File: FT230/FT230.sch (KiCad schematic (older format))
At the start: 19 parts, among them J1 USB_B_Micro, J2 Conn_01x04, J3 Conn_01x02, J4 Conn_01x02, U1 FT230XQ

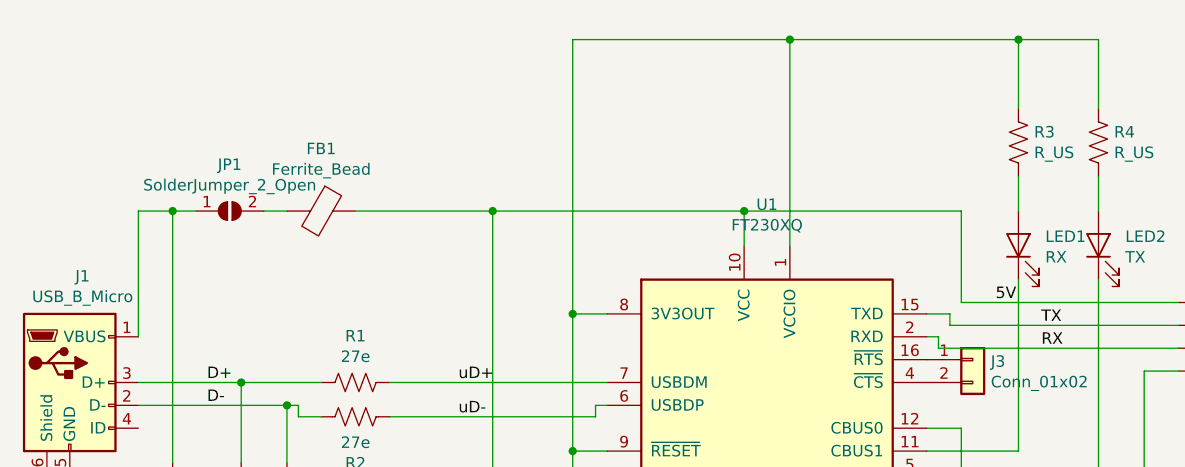
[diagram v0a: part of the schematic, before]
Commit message: Silkscreens Updated
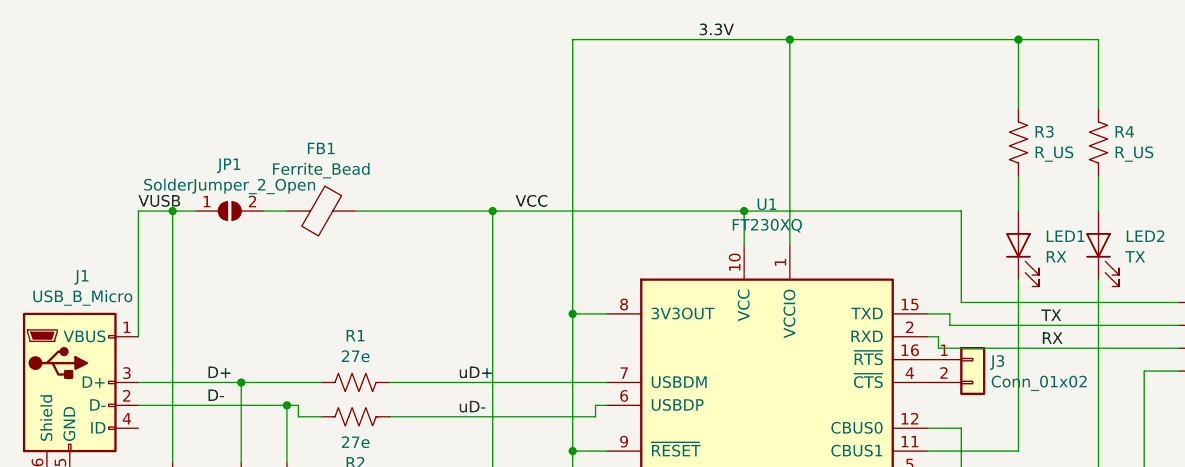
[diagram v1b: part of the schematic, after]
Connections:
- net 3.3V: now reaches C6.1, R3.1, R4.1, U1.1 (VCCIO), U1.8 (3V3OUT), U1.9 (~RESET)
- net VUSB: now reaches C1.1, J1.1 (VBUS), JP1.1 (A)
- net 5V renamed VCC
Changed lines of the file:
@@
 Text Label 6000 2950 0    50   ~ 0
 TX
-Text Label 5800 2850 0    50   ~ 0
-5V
+Text Label 2050 2450 0    50   ~ 0
+VUSB
 Wire Wire Line
 	6450 3150 6450 4200
@@
 Wire Wire Line
 	4700 2450 5650 2450
+Text Label 4500 1700 0    50   ~ 0
+3.3V
+Text Label 3700 2450 0    50   ~ 0
+VCC
 $EndSCHEMATC

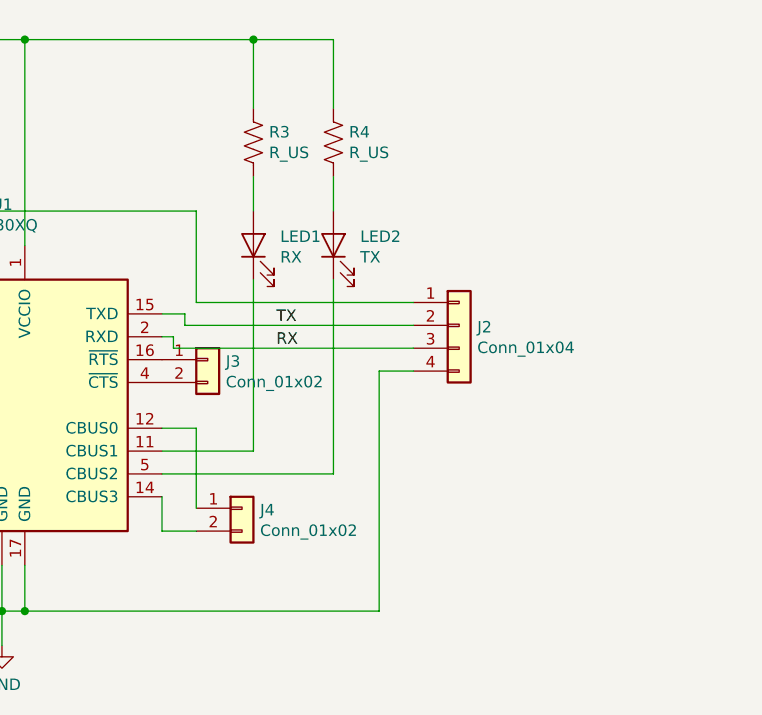
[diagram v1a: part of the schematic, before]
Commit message: Power LED Added
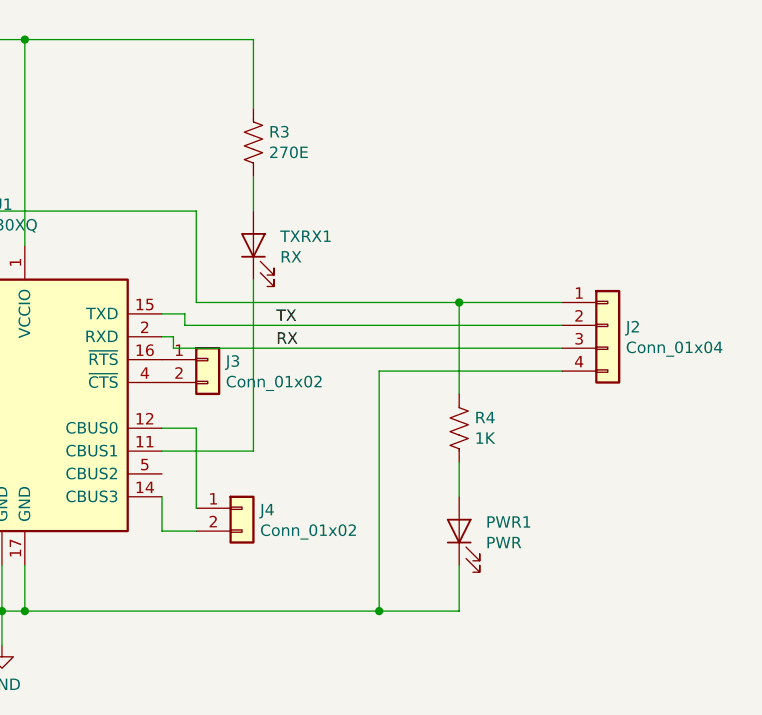
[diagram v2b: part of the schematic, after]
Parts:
- PWR1: renamed from LED2; value TX -> PWR
- R3: value R_US -> 270E
- R4: value R_US -> 1K
- renumbered LED1 to TXRX1
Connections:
- net 3.3V: no longer R4.1
- net GND: now also PWR1.1 (K)
- net VCC: now also R4.1
- net at U1.5 (CBUS2): no longer PWR1.1 (K)
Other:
- moved on the sheet: J2, PWR1, R4
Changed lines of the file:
@@
-$EndComp
-$Comp
-L Device:R_US R4
-U 1 1 5D279F68
-P 6250 2150
-F 0 "R4" H 6318 2195 50  0000 L CNN
-F 1 "R_US" H 6318 2105 50  0000 L CNN
-F 2 "Resistor_SMD:R_0805_2012Metric_Pad1.15x1.40mm_HandSolder" V 6290 2140 50  0001 C CNN
-F 3 "~" H 6250 2150 50  0001 C CNN
-	1    6250 2150
-	1    0    0    -1
 $EndComp
 $Comp
@@
 	4700 4200 4700 4000
 $Comp
-L Device:LED LED2
-U 1 1 5D27B0C2
-P 6250 2600
-F 0 "LED2" V 6288 2483 50  0000 R CNN
-F 1 "TX" V 6198 2483 50  0000 R CNN
-F 2 "LED_SMD:LED_0805_2012Metric_Castellated" H 6250 2600 50  0001 C CNN
-F 3 "~" H 6250 2600 50  0001 C CNN
-	1    6250 2600
-	0    -1   -1   0
-$EndComp
-$Comp
 L Device:R_US R3
 U 1 1 5D282FE6
 P 5900 2150
 F 0 "R3" H 5968 2195 50  0000 L CNN
-F 1 "R_US" H 5968 2105 50  0000 L CNN
+F 1 "270E" H 5968 2105 50  0000 L CNN
 F 2 "Resistor_SMD:R_0805_2012Metric_Pad1.15x1.40mm_HandSolder" V 5940 2140 50  0001 C CNN
 F 3 "~" H 5900 2150 50  0001 C CNN
@@
 $EndComp
 $Comp
-L Device:LED LED1
+L Device:LED TXRX1
 U 1 1 5D282FEC
 P 5900 2600
-F 0 "LED1" V 5938 2483 50  0000 R CNN
+F 0 "TXRX1" V 5938 2483 50  0000 R CNN
 F 1 "RX" V 5848 2483 50  0000 R CNN
 F 2 "LED_SMD:LED_0805_2012Metric_Castellated" H 5900 2600 50  0001 C CNN
@@
 	5900 3500 5500 3500
 Wire Wire Line
-	6250 2300 6250 2450
-Wire Wire Line
-	6250 2750 6250 3600
-Wire Wire Line
-	6250 3600 5500 3600
-Wire Wire Line
 	4900 2600 4900 1700
 Wire Wire Line
 	4900 1700 5900 1700
 Wire Wire Line
-	6250 1700 6250 2000
-Wire Wire Line
 	5900 2000 5900 1700
-Connection ~ 5900 1700
-Wire Wire Line
-	5900 1700 6250 1700
 Wire Wire Line
 	4100 3500 3950 3500
@@
 L Connector_Generic:Conn_01x04 J2
 U 1 1 5D2DAFBA
-P 6800 2950
-F 0 "J2" H 6879 2942 50  0000 L CNN
-F 1 "Conn_01x04" H 6879 2852 50  0000 L CNN
-F 2 "Connector_PinHeader_2.54mm:PinHeader_1x04_P2.54mm_Horizontal" H 6800 2950 50  0001 C CNN
-F 3 "~" H 6800 2950 50  0001 C CNN
-	1    6800 2950
+P 7450 2950
+F 0 "J2" H 7529 2942 50  0000 L CNN
+F 1 "Conn_01x04" H 7529 2852 50  0000 L CNN
+F 2 "Connector_PinHeader_2.54mm:PinHeader_1x04_P2.54mm_Horizontal" H 7450 2950 50  0001 C CNN
+F 3 "~" H 7450 2950 50  0001 C CNN
+	1    7450 2950
 	1    0    0    -1
 $EndComp
@@
 	5650 2850 5650 2450
 Wire Wire Line
-	5650 2850 6600 2850
-Wire Wire Line
-	6600 2950 5600 2950
+	5650 2850 6800 2850
+Wire Wire Line
+	7250 2950 5600 2950
 Wire Wire Line
 	5600 2950 5600 2900
@@
 	5550 3000 5550 3050
 Wire Wire Line
-	5550 3050 6600 3050
+	5550 3050 7250 3050
 Wire Wire Line
 	4900 4200 6450 4200
 Wire Wire Line
-	6450 3150 6600 3150
+	6450 3150 7250 3150
 Connection ~ 4900 4200
 Text Label 2350 3200 0    50   ~ 0
@@
 Text Label 3700 2450 0    50   ~ 0
 VCC
+Wire Wire Line
+	6800 3550 6800 3700
+$Comp
+L Device:LED PWR1
+U 1 1 5D27B0C2
+P 6800 3850
+F 0 "PWR1" V 6838 3733 50  0000 R CNN
+F 1 "PWR" V 6748 3733 50  0000 R CNN
+F 2 "LED_SMD:LED_0805_2012Metric_Castellated" H 6800 3850 50  0001 C CNN
+F 3 "~" H 6800 3850 50  0001 C CNN
+	1    6800 3850
+	0    -1   -1   0
+$EndComp
+$Comp
+L Device:R_US R4
+U 1 1 5D279F68
+P 6800 3400
+F 0 "R4" H 6868 3445 50  0000 L CNN
+F 1 "1K" H 6868 3355 50  0000 L CNN
+F 2 "Resistor_SMD:R_0805_2012Metric_Pad1.15x1.40mm_HandSolder" V 6840 3390 50  0001 C CNN
+F 3 "~" H 6800 3400 50  0001 C CNN
+	1    6800 3400
+	1    0    0    -1
+$EndComp
+Wire Wire Line
+	6800 3250 6800 2850
+Connection ~ 6800 2850
+Wire Wire Line
+	6800 2850 7250 2850
+Wire Wire Line
+	6800 4000 6800 4200
+Wire Wire Line
+	6800 4200 6450 4200
+Connection ~ 6450 4200
 $EndSCHEMATC

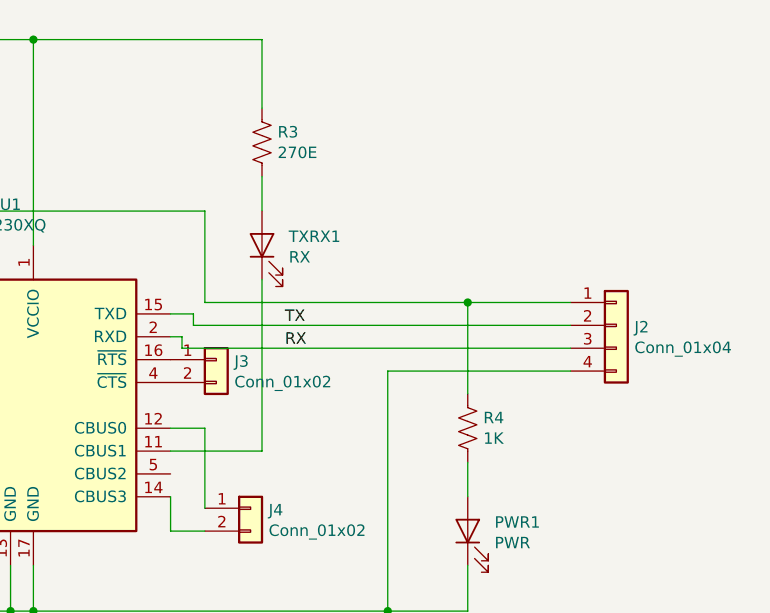
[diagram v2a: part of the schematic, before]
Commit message: Power LED edited
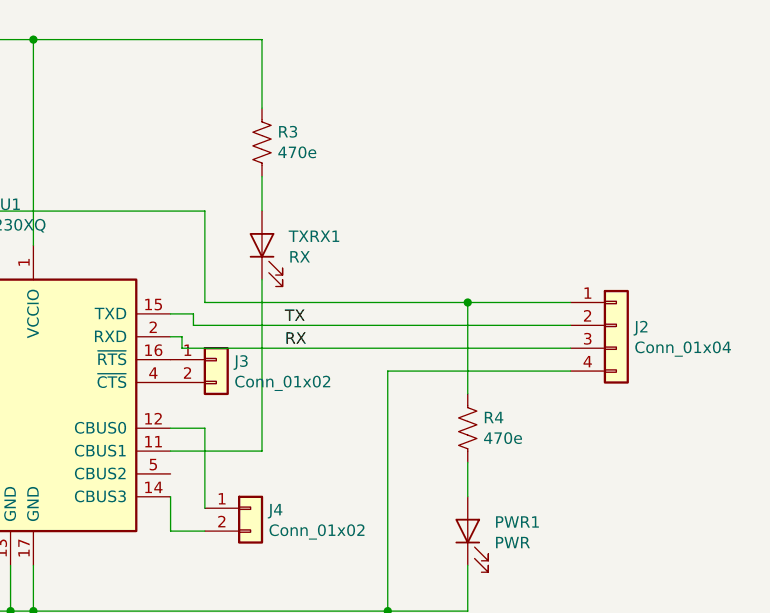
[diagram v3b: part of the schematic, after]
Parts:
- R3: value 270E -> 470e
- R4: value 1K -> 470e
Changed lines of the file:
@@
 P 5900 2150
 F 0 "R3" H 5968 2195 50  0000 L CNN
-F 1 "270E" H 5968 2105 50  0000 L CNN
+F 1 "470e" H 5968 2105 50  0000 L CNN
 F 2 "Resistor_SMD:R_0805_2012Metric_Pad1.15x1.40mm_HandSolder" V 5940 2140 50  0001 C CNN
 F 3 "~" H 5900 2150 50  0001 C CNN
@@
 P 6800 3400
 F 0 "R4" H 6868 3445 50  0000 L CNN
-F 1 "1K" H 6868 3355 50  0000 L CNN
+F 1 "470e" H 6868 3355 50  0000 L CNN
 F 2 "Resistor_SMD:R_0805_2012Metric_Pad1.15x1.40mm_HandSolder" V 6840 3390 50  0001 C CNN
 F 3 "~" H 6800 3400 50  0001 C CNN

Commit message: Page Settings Updated
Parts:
- FB1: value Ferrite_Bead -> 40E@100MHz
- PWR1: value PWR -> RED
- TXRX1: value RX -> GREEN
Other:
- moved on the sheet: C1, C2, C3, C4, C5, C6, FB1, J1, J2, J3, J4, JP1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

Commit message: Part Numbers Added
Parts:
- C1: footprint Capacitor_SMD:C_0805_2012Metric_Pad1.15x1.40mm_HandSolder -> Capacitor_SMD:C_0603_1608Metric; Part (none) -> C100042
- C2, C3: footprint Capacitor_SMD:C_0805_2012Metric_Pad1.15x1.40mm_HandSolder -> Capacitor_SMD:C_0603_1608Metric; Part (none) -> C105622
- C4, C6: footprint Capacitor_SMD:C_0805_2012Metric_Pad1.15x1.40mm_HandSolder -> Capacitor_SMD:C_0603_1608Metric; Part (none) -> C42998
- C5: Part (none) -> C87998
- FB1: footprint Inductor_SMD:L_0805_2012Metric_Pad1.15x1.40mm_HandSolder -> Inductor_SMD:L_0603_1608Metric; Part (none) -> C53139
- J1: Part (none) -> C132560
- PWR1: footprint LED_SMD:LED_0805_2012Metric_Castellated -> LED_SMD:LED_0603_1608Metric; Part (none) -> C118330
- R1, R2: footprint Resistor_SMD:R_0805_2012Metric_Pad1.15x1.40mm_HandSolder -> Resistor_SMD:R_0603_1608Metric; Part (none) -> C325726
- R3: value 470e -> 680E; footprint Resistor_SMD:R_0805_2012Metric_Pad1.15x1.40mm_HandSolder -> Resistor_SMD:R_0603_1608Metric; Part (none) -> C269441
- R4: value 470e -> 680E; Part (none) -> C269441
- TXRX1: footprint LED_SMD:LED_0805_2012Metric_Castellated -> LED_SMD:LED_0603_1608Metric; Part (none) -> C205443
- U1: Part (none) -> 888-8716
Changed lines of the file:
@@
 F 2 "Package_DFN_QFN:QFN-16-1EP_4x4mm_P0.65mm_EP2.1x2.1mm" H 4800 1875 50  0001 C CNN
 F 3 "http://www.ftdichip.com/Products/ICs/FT230X.html" H 4250 2575 50  0001 C CNN
+F 4 "888-8716" H 4250 2575 50  0001 C CNN "Part"
 	1    4250 2575
 	1    0    0    -1
@@
 F 0 "C6" H 3475 3325 50  0000 L CNN
 F 1 "100nF" H 3475 3125 50  0000 L CNN
-F 2 "Capacitor_SMD:C_0805_2012Metric_Pad1.15x1.40mm_HandSolder" H 3438 3075 50  0001 C CNN
+F 2 "Capacitor_SMD:C_0603_1608Metric" H 3438 3075 50  0001 C CNN
 F 3 "~" H 3400 3225 50  0001 C CNN
+F 4 "C42998" H 3400 3225 50  0001 C CNN "Part"
 	1    3400 3225
 	1    0    0    -1
@@
 F 2 "Capacitor_SMD:C_0805_2012Metric_Pad1.15x1.40mm_HandSolder" H 3088 3075 50  0001 C CNN
 F 3 "~" H 3050 3225 50  0001 C CNN
+F 4 "C87998" H 3050 3225 50  0001 C CNN "Part"
 	1    3050 3225
 	1    0    0    -1
@@
 P 5350 1425
 F 0 "R3" H 5418 1470 50  0000 L CNN
-F 1 "470e" H 5418 1380 50  0000 L CNN
-F 2 "Resistor_SMD:R_0805_2012Metric_Pad1.15x1.40mm_HandSolder" V 5390 1415 50  0001 C CNN
+F 1 "680E" H 5418 1380 50  0000 L CNN
+F 2 "Resistor_SMD:R_0603_1608Metric" V 5390 1415 50  0001 C CNN
 F 3 "~" H 5350 1425 50  0001 C CNN
+F 4 "C269441" H 5350 1425 50  0001 C CNN "Part"
 	1    5350 1425
 	1    0    0    -1
@@
 F 0 "TXRX1" V 5388 1758 50  0000 R CNN
 F 1 "GREEN" V 5298 1758 50  0000 R CNN
-F 2 "LED_SMD:LED_0805_2012Metric_Castellated" H 5350 1875 50  0001 C CNN
+F 2 "LED_SMD:LED_0603_1608Metric" H 5350 1875 50  0001 C CNN
 F 3 "~" H 5350 1875 50  0001 C CNN
+F 4 "C205443" V 5350 1875 50  0001 C CNN "Part"
 	1    5350 1875
 	0    -1   -1   0
@@
 F 2 "Connector_USB:USB_Micro-B_Molex_47346-0001" H 1350 2425 50  0001 C CNN
 F 3 "~" H 1350 2425 50  0001 C CNN
+F 4 "C132560" H 1200 2475 50  0001 C CNN "Part"
 	1    1200 2475
 	1    0    0    -1
@@
 F 0 "R1" V 2653 2475 50  0000 C CNN
 F 1 "27e" V 2563 2475 50  0000 C CNN
-F 2 "Resistor_SMD:R_0805_2012Metric_Pad1.15x1.40mm_HandSolder" V 2490 2465 50  0001 C CNN
+F 2 "Resistor_SMD:R_0603_1608Metric" V 2490 2465 50  0001 C CNN
 F 3 "~" H 2450 2475 50  0001 C CNN
+F 4 "C325726" V 2450 2475 50  0001 C CNN "Part"
 	1    2450 2475
 	0    -1   -1   0
@@
 F 0 "R2" V 2653 2625 50  0000 C CNN
 F 1 "27e" V 2563 2625 50  0000 C CNN
-F 2 "Resistor_SMD:R_0805_2012Metric_Pad1.15x1.40mm_HandSolder" V 2490 2615 50  0001 C CNN
+F 2 "Resistor_SMD:R_0603_1608Metric" V 2490 2615 50  0001 C CNN
 F 3 "~" H 2450 2625 50  0001 C CNN
+F 4 "C325726" V 2450 2625 50  0001 C CNN "Part"
 	1    2450 2625
 	0    1    1    0
@@
 F 0 "C3" H 2200 3075 50  0000 L CNN
 F 1 "47pF" H 2200 2875 50  0000 L CNN
-F 2 "Capacitor_SMD:C_0805_2012Metric_Pad1.15x1.40mm_HandSolder" H 2188 2825 50  0001 C CNN
+F 2 "Capacitor_SMD:C_0603_1608Metric" H 2188 2825 50  0001 C CNN
 F 3 "~" H 2150 2975 50  0001 C CNN
+F 4 "C105622" H 2150 2975 50  0001 C CNN "Part"
 	1    2150 2975
 	1    0    0    -1
@@
 F 0 "C2" H 2000 3075 50  0000 L CNN
 F 1 "47pF" H 2000 2875 50  0000 L CNN
-F 2 "Capacitor_SMD:C_0805_2012Metric_Pad1.15x1.40mm_HandSolder" H 1988 2825 50  0001 C CNN
+F 2 "Capacitor_SMD:C_0603_1608Metric" H 1988 2825 50  0001 C CNN
 F 3 "~" H 1950 2975 50  0001 C CNN
+F 4 "C105622" H 1950 2975 50  0001 C CNN "Part"
 	1    1950 2975
 	-1   0    0    -1
@@
 F 0 "C4" H 2750 3325 50  0000 R CNN
 F 1 "100nF" H 2750 3125 50  0000 R CNN
-F 2 "Capacitor_SMD:C_0805_2012Metric_Pad1.15x1.40mm_HandSolder" H 2838 3075 50  0001 C CNN
+F 2 "Capacitor_SMD:C_0603_1608Metric" H 2838 3075 50  0001 C CNN
 F 3 "~" H 2800 3225 50  0001 C CNN
+F 4 "C42998" H 2800 3225 50  0001 C CNN "Part"
 	1    2800 3225
 	1    0    0    -1
@@
 F 0 "C1" H 1600 3075 50  0000 R CNN
 F 1 "10nF" H 1600 2875 50  0000 R CNN
-F 2 "Capacitor_SMD:C_0805_2012Metric_Pad1.15x1.40mm_HandSolder" H 1688 2825 50  0001 C CNN
+F 2 "Capacitor_SMD:C_0603_1608Metric" H 1688 2825 50  0001 C CNN
 F 3 "~" H 1650 2975 50  0001 C CNN
+F 4 "C100042" H 1650 2975 50  0001 C CNN "Part"
 	1    1650 2975
 	1    0    0    -1
@@
 F 0 "FB1" V 2028 1725 50  0000 C CNN
 F 1 "40E@100MHz" V 2118 1725 50  0000 C CNN
-F 2 "Inductor_SMD:L_0805_2012Metric_Pad1.15x1.40mm_HandSolder" V 2230 1725 50  0001 C CNN
+F 2 "Inductor_SMD:L_0603_1608Metric" V 2230 1725 50  0001 C CNN
 F 3 "~" H 2300 1725 50  0001 C CNN
+F 4 "C53139" V 2300 1725 50  0001 C CNN "Part"
 	1    2300 1725
 	0    1    1    0
@@
 F 0 "PWR1" V 6288 3008 50  0000 R CNN
 F 1 "RED" V 6198 3008 50  0000 R CNN
-F 2 "LED_SMD:LED_0805_2012Metric_Castellated" H 6250 3125 50  0001 C CNN
+F 2 "LED_SMD:LED_0603_1608Metric" H 6250 3125 50  0001 C CNN
 F 3 "~" H 6250 3125 50  0001 C CNN
+F 4 "C118330" V 6250 3125 50  0001 C CNN "Part"
 	1    6250 3125
 	0    -1   -1   0
@@
 P 6250 2675
 F 0 "R4" H 6318 2720 50  0000 L CNN
-F 1 "470e" H 6318 2630 50  0000 L CNN
+F 1 "680E" H 6318 2630 50  0000 L CNN
 F 2 "Resistor_SMD:R_0805_2012Metric_Pad1.15x1.40mm_HandSolder" V 6290 2665 50  0001 C CNN
 F 3 "~" H 6250 2675 50  0001 C CNN
+F 4 "C269441" H 6250 2675 50  0001 C CNN "Part"
 	1    6250 2675
 	1    0    0    -1
